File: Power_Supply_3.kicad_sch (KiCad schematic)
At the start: 12 parts

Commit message: VER2.2: все изменения в списке изменений
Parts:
- removed D10, D18: WRA1215S-3WR2, Mornsun:WRA_S-3WR2, symbol Morsun:WRA1215S-3WR2
- added D10, D18: ~, DCDC_My:QA, symbol DCDC_My:QA1
- added L11, L12: 12u, Inductor_SMD:L_1210_3225Metric_Pad1.42x2.65mm_HandSolder, symbol Device:L
- C18, C19, C47, C48: value 10u -> 4.7u; footprint Capacitor_SMD:C_1210_3225Metric_Pad1.33x2.70mm_HandSolder -> Capacitor_SMD:C_1206_3216Metric_Pad1.33x1.80mm_HandSolder
- L4, L6: value 4.7u -> 47u; Product Name (none) -> LQH43CN470K03L
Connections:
- net +15V: now also L11.1, L12.1; no longer L4.1, L6.1
- net +15V_H3: now also D10.7 (+Vo)
- net +15V_L3: now also D18.7 (+Vo)
- net -15V_H3: now also D10.5 (-Vo)
- net -15V_L3: now also D18.5 (-Vo)
- net E5: now also D10.6 (0V)
- net E6: now also D18.6 (0V)
- net GND: now also D10.2 (GND), D18.2 (GND)
- net at C19.1: now also L4.1, L11.2; no longer L4.2
- net at C48.1: now also L6.1, L12.2; no longer L6.2
- new net: D10.1 (Vin), L4.2
- new net: D18.1 (Vin), L6.2
- no-connect marks 2 -> 0
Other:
- moved on the sheet: C17, C18, C19, C20, C44, C47, C48, C49, L4, L6

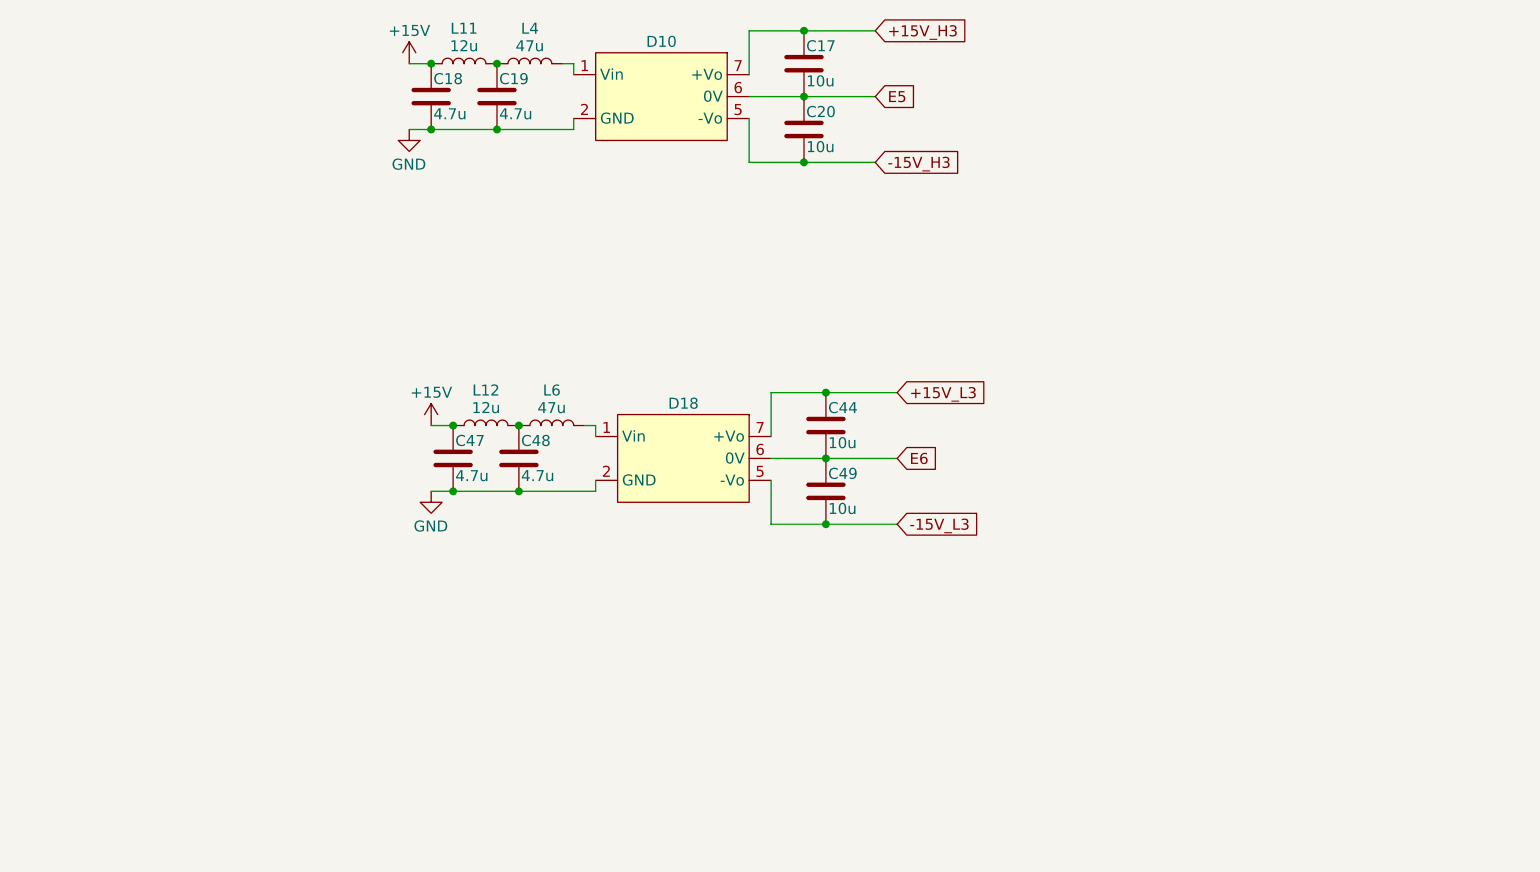
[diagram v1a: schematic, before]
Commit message: VER2.2: добавил фильтры на вход ШИМа и обновил все доки
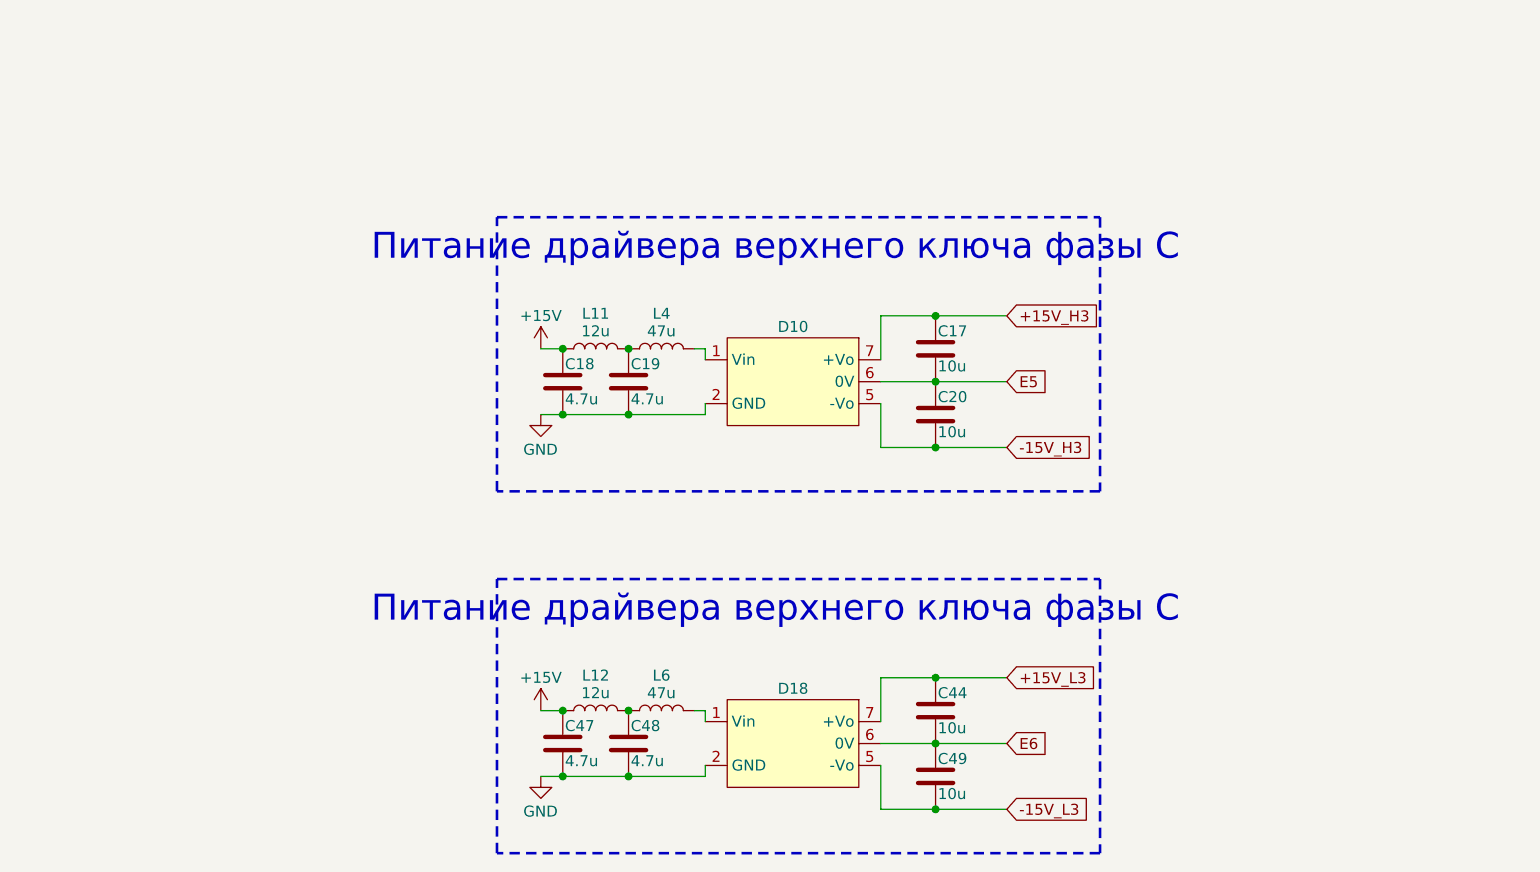
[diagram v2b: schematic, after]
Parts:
- L11, L12, L4, L6: Description P/N (none) -> Inductor SMD
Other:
- note added: "Питание драйвера верхнего ключа фазы С"
- company: (none) -> ООО "ЭТТ"
- moved on the sheet: C17, C18, C19, C20, C44, C47, C48, C49, D10, D18, L11, L12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

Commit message: VER2.2.1: создал папку для производственных доков
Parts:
- C17, C20, C44, C49: Description P/N (none) -> Capacitor SMD 50+V
- C18, C19, C47, C48: Description P/N (none) -> Capacitor SMD 25+V
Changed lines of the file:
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@@
 			)
 		)
-		(property "Description P/N" ""
+		(property "Description P/N" "Capacitor SMD 25+V"
 			(at 129.54 91.44 0)
 			(effects
@@
 			)
 		)
-		(property "Description P/N" ""
+		(property "Description P/N" "Capacitor SMD 25+V"
 			(at 129.54 133.35 0)
 			(effects
@@
 			)
 		)
-		(property "Description P/N" ""
+		(property "Description P/N" "Capacitor SMD 25+V"
 			(at 137.16 91.44 0)
 			(effects
@@
 			)
 		)
-		(property "Description P/N" ""
+		(property "Description P/N" "Capacitor SMD 25+V"
 			(at 137.16 133.35 0)
 			(effects
@@
 			)
 		)
-		(property "Description P/N" ""
+		(property "Description P/N" "Capacitor SMD 50+V"
 			(at 172.72 87.63 0)
 			(effects
@@
 			)
 		)
-		(property "Description P/N" ""
+		(property "Description P/N" "Capacitor SMD 50+V"
 			(at 172.72 137.16 0)
 			(effects
@@
 			)
 		)
-		(property "Description P/N" ""
+		(property "Description P/N" "Capacitor SMD 50+V"
 			(at 172.72 129.54 0)
 			(effects
@@
 			)
 		)
-		(property "Description P/N" ""
+		(property "Description P/N" "Capacitor SMD 50+V"
 			(at 172.72 95.25 0)
 			(effects

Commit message: VER2.2.1: исправил все доки
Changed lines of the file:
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@@
 		(date "2025-06-04")
 		(company "ООО \"ЭТТ\"")
+		(comment 1 "НВЦТ.EVP150-2-1.2000.120_v1 Э3")
 	)
 	(rectangle
@@
 					(size 1.27 1.27)
 				)
+				(hide yes)
 			)
 		)
@@
 					(size 1.27 1.27)
 				)
+				(hide yes)
 			)
 		)
@@
 					(size 1.27 1.27)
 				)
+				(hide yes)
 			)
 		)
@@
 					(size 1.27 1.27)
 				)
+				(hide yes)
 			)
 		)
@@
 					(size 1.27 1.27)
 				)
+				(hide yes)
 			)
 		)
@@
 					(size 1.27 1.27)
 				)
+				(hide yes)
 			)
 		)
@@
 					(size 1.27 1.27)
 				)
+				(hide yes)
 			)
 		)
@@
 					(size 1.27 1.27)
 				)
-			)
-		)
+				(hide yes)
+			)
+		)

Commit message: VER2.2: исправил ошибки в доках
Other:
- moved on the sheet: C17, C18, C19, C20, C44, C47, C48, C49, D10, D18, L11, L12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
